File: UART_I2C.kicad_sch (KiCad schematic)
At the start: 26 parts, among them J2 Uart1, J3 Uart4, J4 Uart7, J5 Uart(, J6 Uart6, J7 Uart3

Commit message: Define reusable aliases for hierarchical buses
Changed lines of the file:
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@@
 		)
 	)
-	(hierarchical_label "UART7{UART}"
+	(hierarchical_label "UART7{UART_FLOW}"
 		(shape input)
 		(at 29.21 71.12 180)

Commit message: update powersupplie
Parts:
- removed C37: 10u, Capacitor_SMD:C_0805_2012Metric, symbol FC01_Project:UART_I2C__C_Small
- added C27: 22u, Capacitor_SMD:C_0805_2012Metric, symbol FC01_Project:POWER__C_Small
- added C28: 100n, Capacitor_SMD:C_0402_1005Metric, symbol FC01_Project:POWER__C_Small
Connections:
- net GND: now also C27.2, C28.2
- net +9V renamed +VbatFiltred
- net +VbatFiltred: now also C27.1, C28.1
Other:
- note added: "DJI VIDEO TX"
- moved on the sheet: C36, C38, C39, C40, C41, J2, J3, J4, J5, J6, J7, R20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

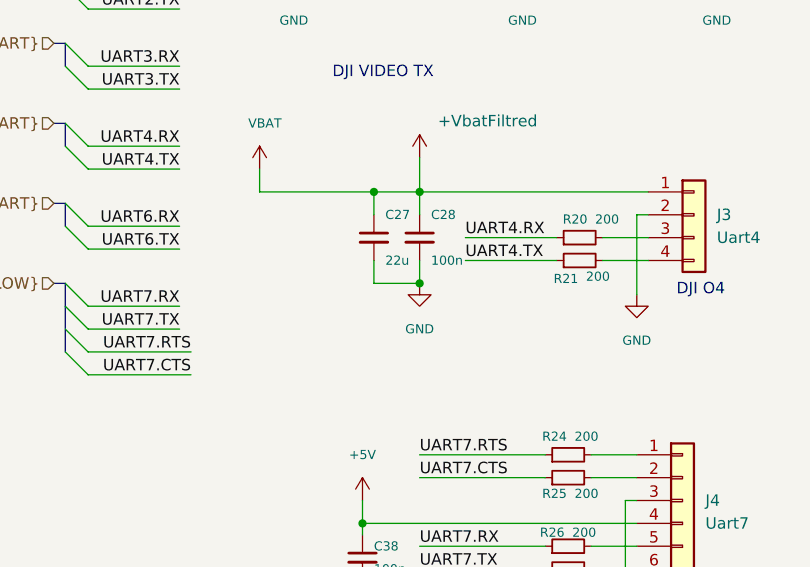
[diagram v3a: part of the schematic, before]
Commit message: Update C27 to 22uF 35V X7R in 1210
Use Samsung CL32B226KLV6PJE (22uF, +/-10%, 35V, X7R) for C27 in UART_I2C. Add a visible Tension nominale field and dielectric/tolerance properties. Link the exact manufacturer specsheet and clear purchasing data belonging to the old CL21A226 part. Add project-local generic KiCad 1210 footprint and STEP assets.

Manufacturer source: https://product.samsungsem.com/mlcc/CL32B226KLV6PJ.do
Footprint source: https://gitlab.com/kicad/libraries/kicad-footprints/-/raw/master/Capacitor_SMD.pretty/C_1210_3225Metric.kicad_mod
STEP source: https://raw.githubusercontent.com/KiCad/kicad-packages3D/master/Capacitor_SMD.3dshapes/C_1210_3225Metric.step

Validation: lossless structural comparison confirms only C27 properties change; all schematic connections, symbol UUIDs, pin UUIDs and other instances are unchanged. The local 1210 footprint resolves with pads 1 and 2 and a local generic STEP. git diff --check passes. PCB is not modified.
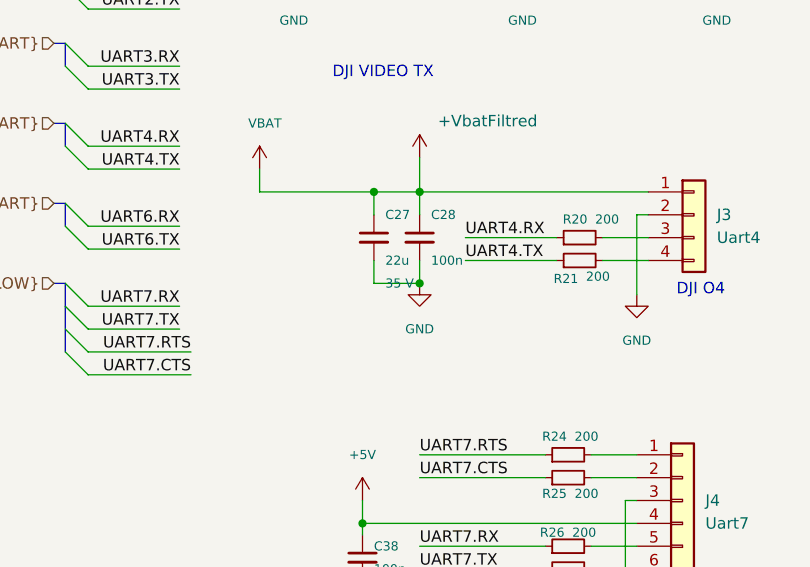
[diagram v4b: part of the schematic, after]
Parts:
- C27: footprint Capacitor_SMD:C_0805_2012Metric -> Capacitor_SMD:C_1210_3225Metric; Component_PDF ${KIPRJMOD}/composants/controle/CL21A226MAYNNNE.pdf -> (none); Datasheet_URL https://product.samsungsem.com/part/download.do?masterKey=CL21A226MAYNNN&type=specsheet -> https://product.samsungsem.com/part/download.do?masterKey=CL32B226KLV6PJ&type=specsheet; Dielectrique (none) -> X7R; DigiKey Part Number 1276-CL21A226MAYNNNECT-ND -> (none); DigiKey Price Qty 1 -> (none); DigiKey Specs 22 µF ±20%, 25 V, X5R, 0805 -> 22 µF ±10%, 35 V, X7R, 1210; caracteristiques confirmees pa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; DigiKey Status Rupture au releve -> Reference identifiee; prix et stock non releves; DigiKey URL https://www.digikey.fr/fr/products/detail/samsung-electro-m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 -> (none); DigiKey Unit Price EUR 0.27 -> (none); DigiKey_Part_Number 1276-CL21A226MAYNNNECT-ND -> (none); DigiKey_URL https://www.digikey.fr/fr/products/detail/samsung-electro-m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 -> (none); Footprint Audit Fiche famille Samsung: code CL05=0402, CL10=0603, CL21=0805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 -> Samsung CL32B226KLV6PJE: fiche fabricant du 24/09/2025, 22 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; Footprint_File ${KIPRJMOD}/composants/kicad/vendor/Capacitor_SMD.pretty/C_0805_2012Metric.kicad_mod -> ${KIPRJMOD}/composants/kicad/vendor/Capacitor_SMD.pretty/C_1210_3225Metric.kicad_mod; Library Audit Fichiers locaux; voir Component_PDF et verification/REPORT.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 -> Empreinte et STEP generiques 1210 locaux; fiche technique S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; MPN CL21A226MAYNNNE -> CL32B226KLV6PJE; MPN_Status (none) -> Reference et caracteristiques confirmees sur la fiche Samsu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; Model_3D ${KIPRJMOD}/composants/3d/C_0805_2012Metric.step -> ${KIPRJMOD}/composants/3d/C_1210_3225Metric.step; Model_3D_Type KiCad, geometrie generique du boitier -> KiCad, geometrie generique du boitier 1210; pas un modele f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; Package 0805 (2012), max H 1.45 mm -> 1210 (3225 metric), 3.20±0.40 x 2.50+0.35/-0.30 mm, max H 2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; Price Checked 2026-09-27 -> (none); Price_Basis EUR HT par piece, hors port -> (none); Price_Checked 2026-09-27 -> (none); Price_Qty 1 -> (none); Stock_Checked 2026-09-27 -> (none); Stock_Units 0 -> (none); Supplier DigiKey France -> (none); Supplier_Notes Relevé web; stock et prix variables. -> Selection du 04/10/2026 selon 22 µF / 35 V / X7R et plus pe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; Supplier_Order_Code 1276-CL21A226MAYNNNECT-ND -> (none); Supplier_Status Rupture au releve -> Reference identifiee; prix et stock non releves; Supplier_URL https://www.digikey.fr/fr/products/detail/samsung-electro-m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 -> (none); Tension nominale (none) -> 35 V; Tolerance (none) -> ±10%; Unit_Price_EUR 0.27 -> (none)
